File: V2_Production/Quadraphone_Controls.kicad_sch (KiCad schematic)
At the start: 30 parts, among them J1 Conn_01x10_Female, J10 Pitch_In, J11 Mix_Out, J12 Conn_02x04_Odd_Even, J13 Conn_01x04_Male, J14 Conn_01x01_Male, J2 Conn_01x10_Female, J3 Conn_01x10_Female, J4 Conn_01x10_Female, J5 PWM_CV, J6 LFO_IN, J7 PWM_CV_In, J8 Synch_Signal_In, J9 Freq_Mod_In, SW1 Synch_Type, SW2 Output_Type, SW3 Output_Type

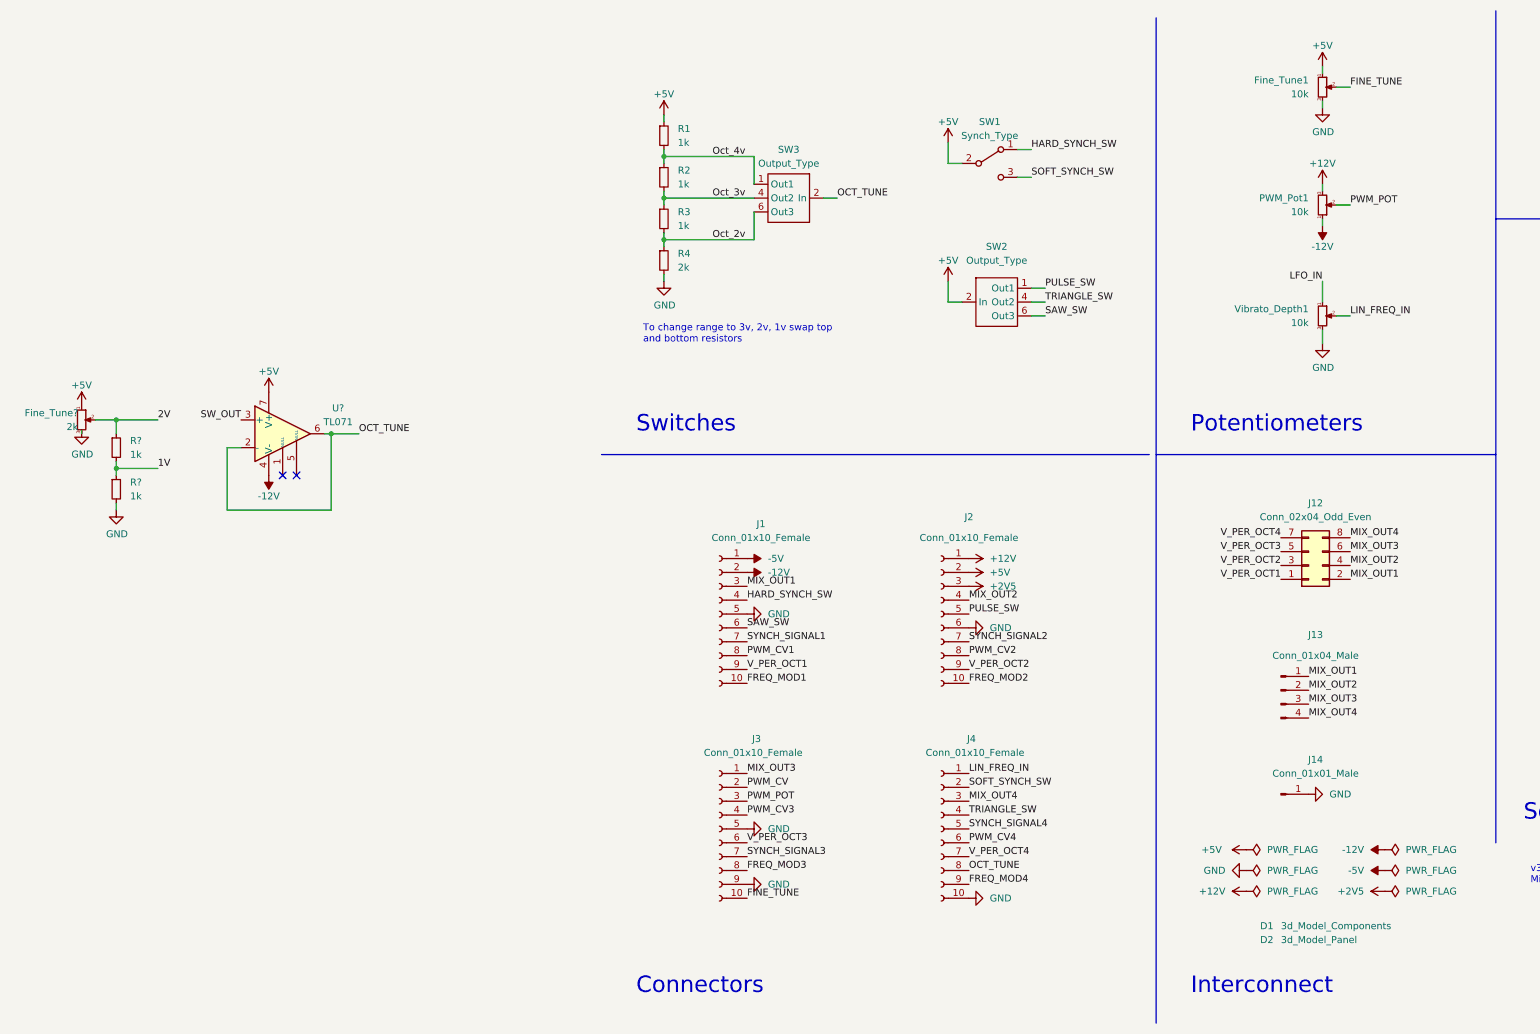
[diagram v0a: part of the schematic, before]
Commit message: Started Rev 3 with buffered octave control
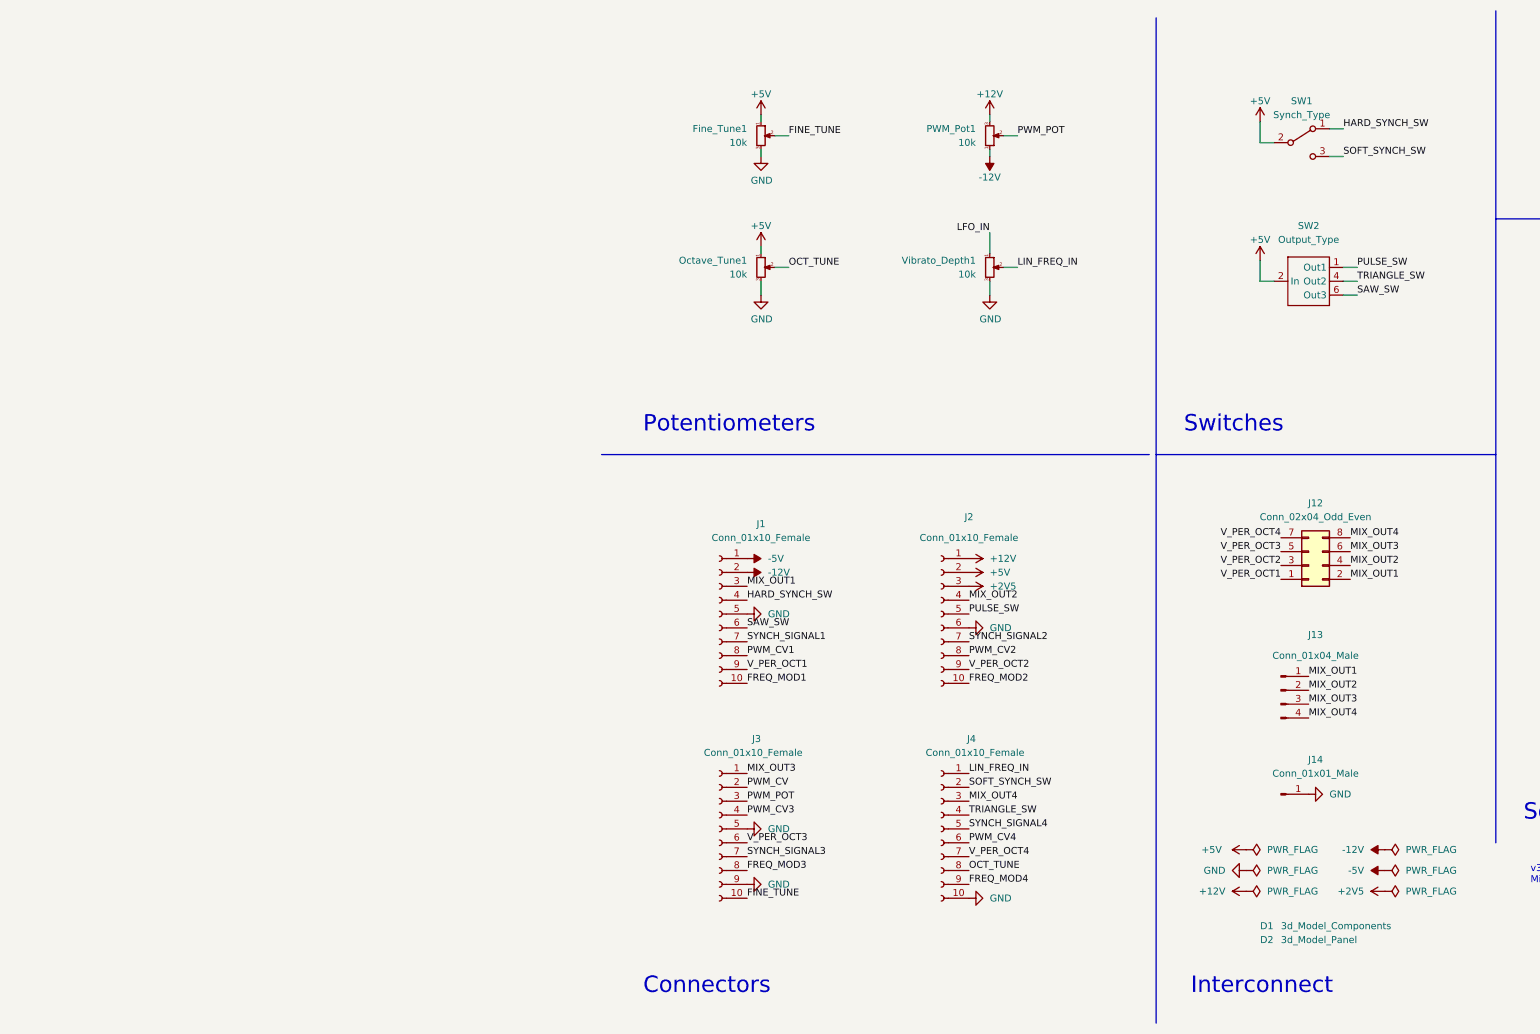
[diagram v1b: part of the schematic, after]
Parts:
- removed Fine_Tune?: 2k, Custom_Footprints:Alpha_9mm_Potentiometer_Aligned, symbol Device:R_Potentiometer_Small
- removed R1, R2, R3, R? (x2): 1k, Resistor_SMD:R_0805_2012Metric, symbol Device:R_Small
- removed R4: 2k, Resistor_SMD:R_0805_2012Metric, symbol Device:R_Small
- removed SW3: Output_Type, Custom_Footprints:100DP6T1B1M2QE_ON_ON_ON, symbol Custom_Audio:DPDT_Switch
- removed U?: TL071, symbol Amplifier_Operational:TL071
- added Octave_Tune1: 10k, Custom_Footprints:Alpha_9mm_Potentiometer_Aligned, symbol Device:R_Potentiometer_Small
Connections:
- net +5V: now also Octave_Tune1.1
- net GND: now also Octave_Tune1.3
- net OCT_TUNE: now also Octave_Tune1.2
- no-connect marks 18 -> 16
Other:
- note removed: "To change range to 3v, 2v, 1v swap top and bottom resistors"
- moved on the sheet: Fine_Tune1, PWM_Pot1, SW1, SW2, Vibrato_Depth1
